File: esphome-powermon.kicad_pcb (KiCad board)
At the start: 2 copper layers, 32 x 55.8 mm, 61 parts, among them J1 Conn_01x15_Female, J11 Conn_01x15_Male, J12 Conn_01x15_Male, J13 Conn_01x04_Pin, J14 Conn_01x02_Pin, J15 Conn_01x04_Pin, J2 Conn_01x15_Female, J3 Conn_01x04_Pin, J4 Conn_01x02_Pin, J5 Conn_01x04_Pin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

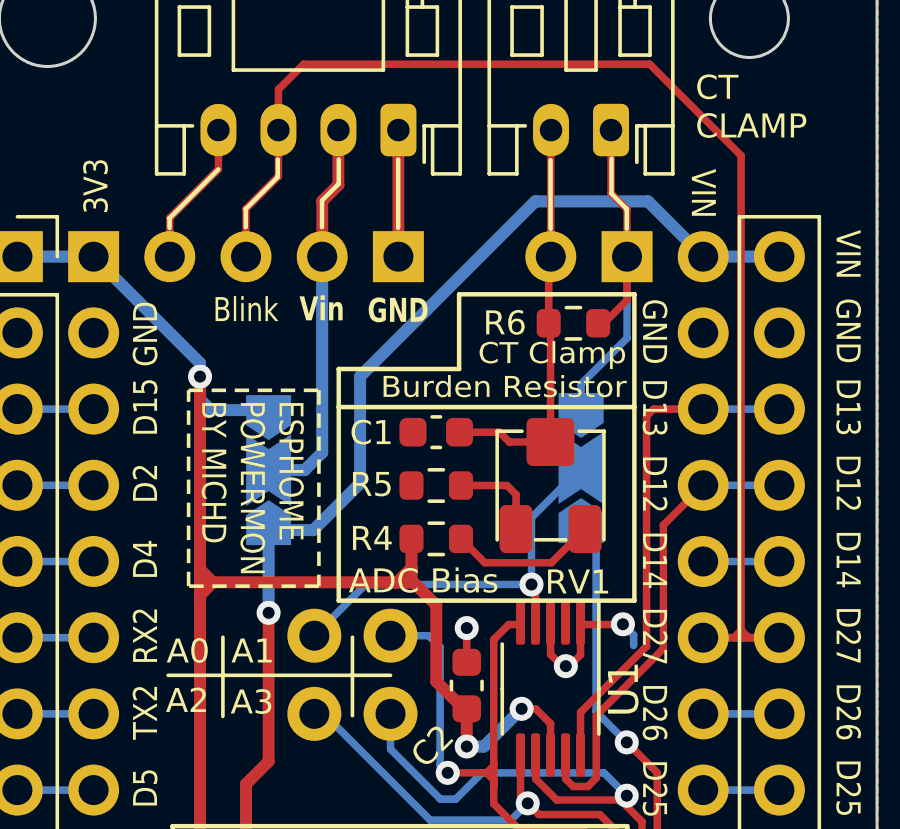
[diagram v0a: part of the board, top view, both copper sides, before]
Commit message: Replace burden resistor with TH footprint
Still for rev0.
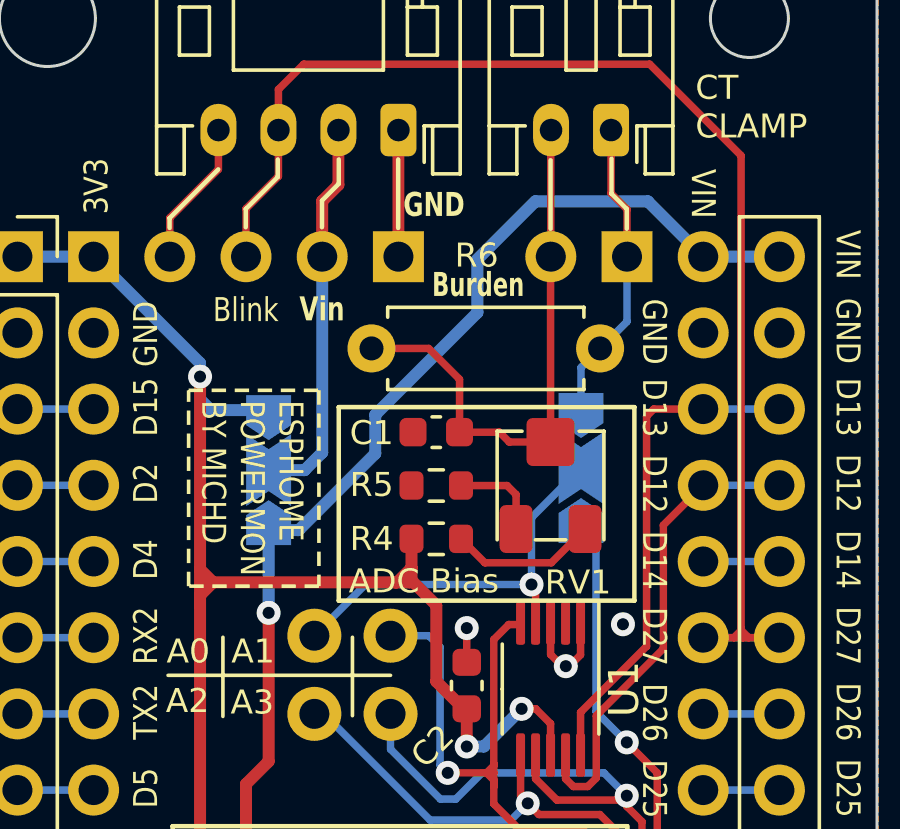
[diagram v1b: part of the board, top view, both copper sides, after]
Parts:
- R6: footprint Resistor_SMD:R_0603_1608Metric -> Resistor_THT:R_Axial_DIN0207_L6.3mm_D2.5mm_P7.62mm_Horizontal
- moved R6 1.22 mm to (153.0, 72.2)
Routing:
- net /CT_CLAMP_2: track 13.6 -> 18.7 mm
- net /CT_CLAMP_1: track 12.9 -> 10.1 mm
- net GND: track 10.8 -> 8.59 mm
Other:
- board text added: "Burden"
- board text removed: "CT Clamp Burden Resistor"
